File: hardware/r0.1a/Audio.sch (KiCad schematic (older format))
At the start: 77 parts, among them J4 MBIAS, J5 TX_Trim, J6 Kenwood-2.5, J7 Radio, J8 Kenwood-3.5, Q1 IRLML2060, U5 LM386, U6 MCP6002-xSN, U7 MCP6002-xSN, U8 LMV341

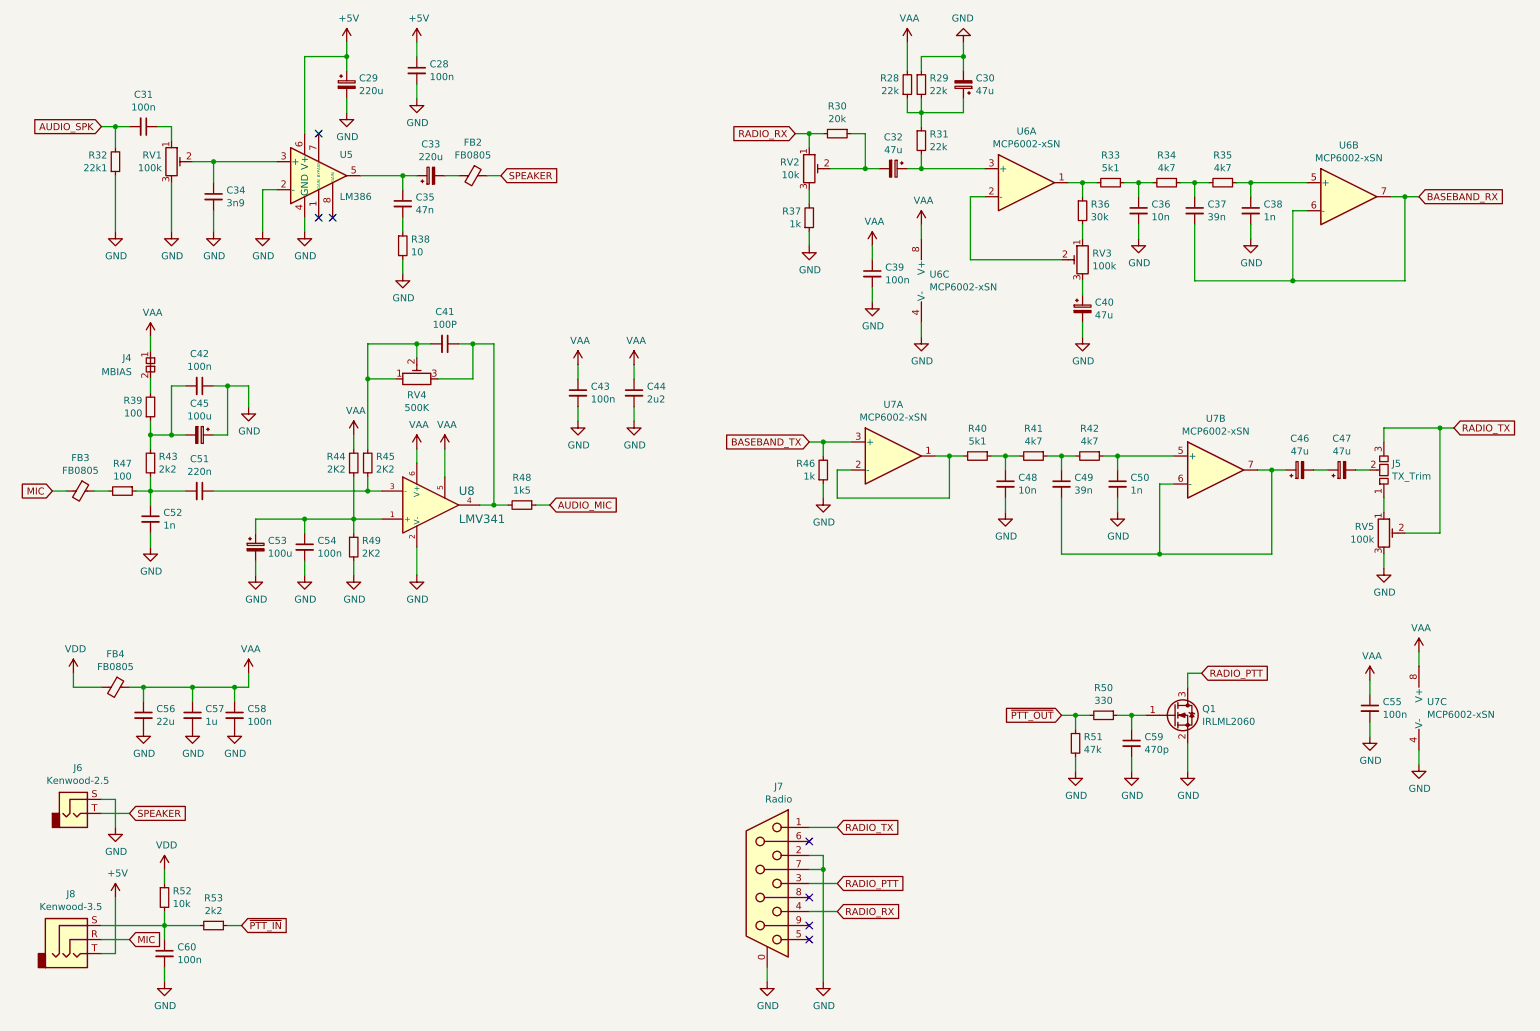
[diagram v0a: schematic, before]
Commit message: Simplified values of R32 and C46,47
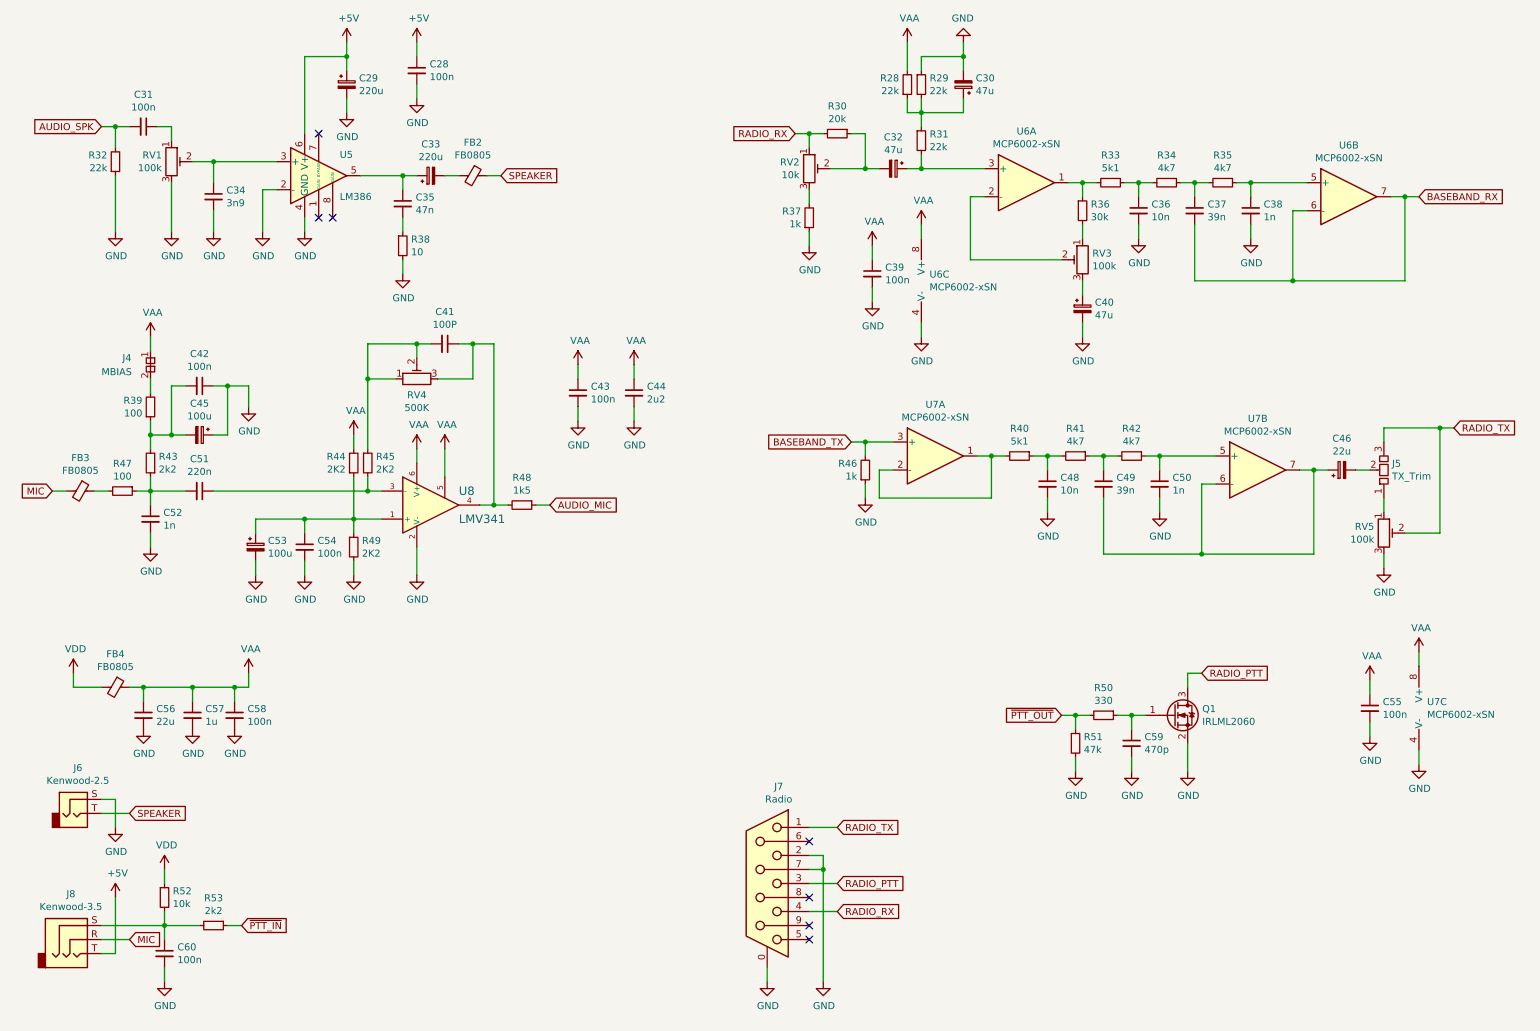
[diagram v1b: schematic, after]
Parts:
- removed C47: 47u, symbol pkl_device:pkl_CP_Small
- C46: value 47u -> 22u
- R32: value 22k1 -> 22k
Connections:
- net at C46.2: now also J5.2
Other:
- moved on the sheet: C46, C48, C49, C50, R40, R41, R42, R46, U7A, U7B
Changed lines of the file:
@@
 P 1200 1650
 F 0 "R32" H 1142 1604 50  0000 R CNN
-F 1 "22k1" H 1142 1695 50  0000 R CNN
+F 1 "22k" H 1142 1695 50  0000 R CNN
 F 2 "" H 1200 1650 60  0000 C CNN
 F 3 "" H 1200 1650 60  0000 C CNN
@@
 L Amplifier_Operational:MCP6002-xSN U7
 U 1 1 62082D27
-P 6750 3750
-F 0 "U7" H 6750 4117 50  0000 C CNN
-F 1 "MCP6002-xSN" H 6750 4026 50  0000 C CNN
-F 2 "" H 6750 3750 50  0001 C CNN
-F 3 "http://ww1.microchip.com/downloads/en/DeviceDoc/21733j.pdf" H 6750 3750 50  0001 C CNN
-	1    6750 3750
+P 7050 3750
+F 0 "U7" H 7050 4117 50  0000 C CNN
+F 1 "MCP6002-xSN" H 7050 4026 50  0000 C CNN
+F 2 "" H 7050 3750 50  0001 C CNN
+F 3 "http://ww1.microchip.com/downloads/en/DeviceDoc/21733j.pdf" H 7050 3750 50  0001 C CNN
+	1    7050 3750
 	1    0    0    -1
 $EndComp
@@
 L Amplifier_Operational:MCP6002-xSN U7
 U 2 1 62085E4A
-P 9050 3850
-F 0 "U7" H 9050 4217 50  0000 C CNN
-F 1 "MCP6002-xSN" H 9050 4126 50  0000 C CNN
-F 2 "" H 9050 3850 50  0001 C CNN
-F 3 "http://ww1.microchip.com/downloads/en/DeviceDoc/21733j.pdf" H 9050 3850 50  0001 C CNN
-	2    9050 3850
+P 9350 3850
+F 0 "U7" H 9350 4217 50  0000 C CNN
+F 1 "MCP6002-xSN" H 9350 4126 50  0000 C CNN
+F 2 "" H 9350 3850 50  0001 C CNN
+F 3 "http://ww1.microchip.com/downloads/en/DeviceDoc/21733j.pdf" H 9350 3850 50  0001 C CNN
+	2    9350 3850
 	1    0    0    -1
 $EndComp
@@
 L pkl_device:pkl_R_Small R46
 U 1 1 62092BC0
-P 6250 3850
-F 0 "R46" H 6192 3804 50  0000 R CNN
-F 1 "1k" H 6192 3895 50  0000 R CNN
-F 2 "" H 6250 3850 60  0000 C CNN
-F 3 "" H 6250 3850 60  0000 C CNN
-	1    6250 3850
+P 6550 3850
+F 0 "R46" H 6492 3804 50  0000 R CNN
+F 1 "1k" H 6492 3895 50  0000 R CNN
+F 2 "" H 6550 3850 60  0000 C CNN
+F 3 "" H 6550 3850 60  0000 C CNN
+	1    6550 3850
 	1    0    0    1
 $EndComp
 Wire Wire Line
-	6450 3850 6350 3850
-Wire Wire Line
-	6350 3850 6350 4050
-Wire Wire Line
-	6350 4050 7150 4050
-Wire Wire Line
-	7150 4050 7150 3750
-Wire Wire Line
-	7150 3750 7050 3750
-Wire Wire Line
-	6450 3650 6250 3650
-Wire Wire Line
-	6250 3650 6250 3750
+	6750 3850 6650 3850
+Wire Wire Line
+	6650 3850 6650 4050
+Wire Wire Line
+	6650 4050 7450 4050
+Wire Wire Line
+	7450 4050 7450 3750
+Wire Wire Line
+	7450 3750 7350 3750
+Wire Wire Line
+	6750 3650 6550 3650
+Wire Wire Line
+	6550 3650 6550 3750
 $Comp
 L power:GND #PWR089
 U 1 1 620A241C
-P 6250 4050
-F 0 "#PWR089" H 6250 3800 50  0001 C CNN
-F 1 "GND" H 6255 3877 50  0000 C CNN
-F 2 "" H 6250 4050 50  0001 C CNN
-F 3 "" H 6250 4050 50  0001 C CNN
-	1    6250 4050
-	1    0    0    -1
-$EndComp
-Wire Wire Line
-	6250 3950 6250 4050
-Wire Wire Line
-	6250 3650 6150 3650
-Connection ~ 6250 3650
-Text GLabel 6150 3650 0    50   Input ~ 0
+P 6550 4050
+F 0 "#PWR089" H 6550 3800 50  0001 C CNN
+F 1 "GND" H 6555 3877 50  0000 C CNN
+F 2 "" H 6550 4050 50  0001 C CNN
+F 3 "" H 6550 4050 50  0001 C CNN
+	1    6550 4050
+	1    0    0    -1
+$EndComp
+Wire Wire Line
+	6550 3950 6550 4050
+Wire Wire Line
+	6550 3650 6450 3650
+Connection ~ 6550 3650
+Text GLabel 6450 3650 0    50   Input ~ 0
 BASEBAND_TX
 Wire Wire Line
-	7250 3750 7150 3750
-Connection ~ 7150 3750
+	7550 3750 7450 3750
+Connection ~ 7450 3750
 $Comp
 L pkl_device:pkl_R_Small R40
 U 1 1 620C166E
-P 7350 3750
-F 0 "R40" V 7154 3750 50  0000 C CNN
-F 1 "5k1" V 7245 3750 50  0000 C CNN
-F 2 "" H 7350 3750 60  0000 C CNN
-F 3 "" H 7350 3750 60  0000 C CNN
-	1    7350 3750
+P 7650 3750
+F 0 "R40" V 7454 3750 50  0000 C CNN
+F 1 "5k1" V 7545 3750 50  0000 C CNN
+F 2 "" H 7650 3750 60  0000 C CNN
+F 3 "" H 7650 3750 60  0000 C CNN
+	1    7650 3750
 	0    1    1    0
 $EndComp
@@
 L pkl_device:pkl_C_Small C48
 U 1 1 620C1678
-P 7550 3950
-F 0 "C48" H 7642 3996 50  0000 L CNN
-F 1 "10n" H 7642 3905 50  0000 L CNN
-F 2 "" H 7550 3950 60  0000 C CNN
-F 3 "" H 7550 3950 60  0000 C CNN
-	1    7550 3950
-	1    0    0    -1
-$EndComp
-Wire Wire Line
-	7450 3750 7550 3750
-Wire Wire Line
-	7550 3750 7550 3850
+P 7850 3950
+F 0 "C48" H 7942 3996 50  0000 L CNN
+F 1 "10n" H 7942 3905 50  0000 L CNN
+F 2 "" H 7850 3950 60  0000 C CNN
+F 3 "" H 7850 3950 60  0000 C CNN
+	1    7850 3950
+	1    0    0    -1
+$EndComp
+Wire Wire Line
+	7750 3750 7850 3750
+Wire Wire Line
+	7850 3750 7850 3850
 $Comp
 L power:GND #PWR090
 U 1 1 620C1684
-P 7550 4150
-F 0 "#PWR090" H 7550 3900 50  0001 C CNN
-F 1 "GND" H 7555 3977 50  0000 C CNN
-F 2 "" H 7550 4150 50  0001 C CNN
-F 3 "" H 7550 4150 50  0001 C CNN
-	1    7550 4150
-	1    0    0    -1
-$EndComp
-Wire Wire Line
-	7550 4050 7550 4150
+P 7850 4150
+F 0 "#PWR090" H 7850 3900 50  0001 C CNN
+F 1 "GND" H 7855 3977 50  0000 C CNN
+F 2 "" H 7850 4150 50  0001 C CNN
+F 3 "" H 7850 4150 50  0001 C CNN
+	1    7850 4150
+	1    0    0    -1
+$EndComp
+Wire Wire Line
+	7850 4050 7850 4150
 $Comp
 L pkl_device:pkl_R_Small R41
 U 1 1 620C168F
-P 7750 3750
-F 0 "R41" V 7554 3750 50  0000 C CNN
-F 1 "4k7" V 7645 3750 50  0000 C CNN
-F 2 "" H 7750 3750 60  0000 C CNN
-F 3 "" H 7750 3750 60  0000 C CNN
-	1    7750 3750
-	0    1    1    0
-$EndComp
-Wire Wire Line
-	7550 3750 7650 3750
-Connection ~ 7550 3750
+P 8050 3750
+F 0 "R41" V 7854 3750 50  0000 C CNN
+F 1 "4k7" V 7945 3750 50  0000 C CNN
+F 2 "" H 8050 3750 60  0000 C CNN
+F 3 "" H 8050 3750 60  0000 C CNN
+	1    8050 3750
+	0    1    1    0
+$EndComp
+Wire Wire Line
+	7850 3750 7950 3750
+Connection ~ 7850 3750
 $Comp
 L pkl_device:pkl_C_Small C49
 U 1 1 620C169B
-P 7950 3950
-F 0 "C49" H 8042 3996 50  0000 L CNN
-F 1 "39n" H 8042 3905 50  0000 L CNN
-F 2 "" H 7950 3950 60  0000 C CNN
-F 3 "" H 7950 3950 60  0000 C CNN
-	1    7950 3950
+P 8250 3950
+F 0 "C49" H 8342 3996 50  0000 L CNN
+F 1 "39n" H 8342 3905 50  0000 L CNN
+F 2 "" H 8250 3950 60  0000 C CNN
+F 3 "" H 8250 3950 60  0000 C CNN
+	1    8250 3950
 	1    0    0    -1
 $EndComp
@@
 L pkl_device:pkl_R_Small R42
 U 1 1 620C16A5
-P 8150 3750
-F 0 "R42" V 7954 3750 50  0000 C CNN
-F 1 "4k7" V 8045 3750 50  0000 C CNN
-F 2 "" H 8150 3750 60  0000 C CNN
-F 3 "" H 8150 3750 60  0000 C CNN
-	1    8150 3750
-	0    1    1    0
-$EndComp
-Wire Wire Line
-	7850 3750 7950 3750
-Wire Wire Line
-	7950 3750 7950 3850
-Connection ~ 7950 3750
-Wire Wire Line
-	7950 3750 8050 3750
+P 8450 3750
+F 0 "R42" V 8254 3750 50  0000 C CNN
+F 1 "4k7" V 8345 3750 50  0000 C CNN
+F 2 "" H 8450 3750 60  0000 C CNN
+F 3 "" H 8450 3750 60  0000 C CNN
+	1    8450 3750
+	0    1    1    0
+$EndComp
+Wire Wire Line
+	8150 3750 8250 3750
+Wire Wire Line
+	8250 3750 8250 3850
+Connection ~ 8250 3750
+Wire Wire Line
+	8250 3750 8350 3750
 $Comp
 L pkl_device:pkl_C_Small C50
 U 1 1 620C16B3
-P 8350 3950
-F 0 "C50" H 8442 3996 50  0000 L CNN
-F 1 "1n" H 8442 3905 50  0000 L CNN
-F 2 "" H 8350 3950 60  0000 C CNN
-F 3 "" H 8350 3950 60  0000 C CNN
-	1    8350 3950
+P 8650 3950
+F 0 "C50" H 8742 3996 50  0000 L CNN
+F 1 "1n" H 8742 3905 50  0000 L CNN
+F 2 "" H 8650 3950 60  0000 C CNN
+F 3 "" H 8650 3950 60  0000 C CNN
+	1    8650 3950
 	1    0    0    -1
 $EndComp
@@
 L power:GND #PWR091
 U 1 1 620C16BD
-P 8350 4150
-F 0 "#PWR091" H 8350 3900 50  0001 C CNN
-F 1 "GND" H 8355 3977 50  0000 C CNN
-F 2 "" H 8350 4150 50  0001 C CNN
-F 3 "" H 8350 4150 50  0001 C CNN
-	1    8350 4150
-	1    0    0    -1
-$EndComp
-Wire Wire Line
-	8350 4050 8350 4150
-Wire Wire Line
-	7950 4450 7950 4050
-Wire Wire Line
-	8250 3750 8350 3750
-Wire Wire Line
-	8350 3750 8350 3850
-Connection ~ 8350 3750
-Wire Wire Line
-	8350 3750 8750 3750
-Wire Wire Line
-	7950 4450 8650 4450
-Wire Wire Line
-	8650 4450 8650 3950
-Wire Wire Line
-	8650 3950 8750 3950
-Wire Wire Line
-	8650 4450 9450 4450
-Wire Wire Line
-	9450 4450 9450 3850
-Wire Wire Line
-	9450 3850 9350 3850
-Connection ~ 8650 4450
+P 8650 4150
+F 0 "#PWR091" H 8650 3900 50  0001 C CNN
+F 1 "GND" H 8655 3977 50  0000 C CNN
+F 2 "" H 8650 4150 50  0001 C CNN
+F 3 "" H 8650 4150 50  0001 C CNN
+	1    8650 4150
+	1    0    0    -1
+$EndComp
+Wire Wire Line
+	8650 4050 8650 4150
+Wire Wire Line
+	8250 4450 8250 4050
+Wire Wire Line
+	8550 3750 8650 3750
+Wire Wire Line
+	8650 3750 8650 3850
+Connection ~ 8650 3750
+Wire Wire Line
+	8650 3750 9050 3750
+Wire Wire Line
+	8250 4450 8950 4450
+Wire Wire Line
+	8950 4450 8950 3950
+Wire Wire Line
+	8950 3950 9050 3950
+Wire Wire Line
+	8950 4450 9750 4450
+Wire Wire Line
+	9750 4450 9750 3850
+Wire Wire Line
+	9750 3850 9650 3850
+Connection ~ 8950 4450
 $Comp
 L pkl_device:pkl_CP_Small C46
 U 1 1 620F10D5
-P 9650 3850
-F 0 "C46" V 9875 3850 50  0000 C CNN
-F 1 "47u" V 9784 3850 50  0000 C CNN
-F 2 "" H 9650 3850 60  0000 C CNN
-F 3 "" H 9650 3850 60  0000 C CNN
-	1    9650 3850
-	0    -1   -1   0
-$EndComp
-$Comp
-L pkl_device:pkl_CP_Small C47
-U 1 1 620F2790
 P 9950 3850
-F 0 "C47" V 10175 3850 50  0000 C CNN
-F 1 "47u" V 10084 3850 50  0000 C CNN
+F 0 "C46" V 10175 3850 50  0000 C CNN
+F 1 "22u" V 10084 3850 50  0000 C CNN
 F 2 "" H 9950 3850 60  0000 C CNN
 F 3 "" H 9950 3850 60  0000 C CNN
@@
 $EndComp
 Wire Wire Line
-	9450 3850 9550 3850
-Connection ~ 9450 3850
-Wire Wire Line
 	9750 3850 9850 3850
+Connection ~ 9750 3850
 Wire Wire Line
 	10050 3850 10150 3850
